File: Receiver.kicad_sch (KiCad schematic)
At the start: 45 parts, among them J2 UFL, J3 UFL, SW2 TS2306A, U1 ESP32-C3, U11 TPRT9013-33, U12 0479480001, U9 SX1280IMLTRT, Y1 40MHz, Y2 52MHz/10ppm

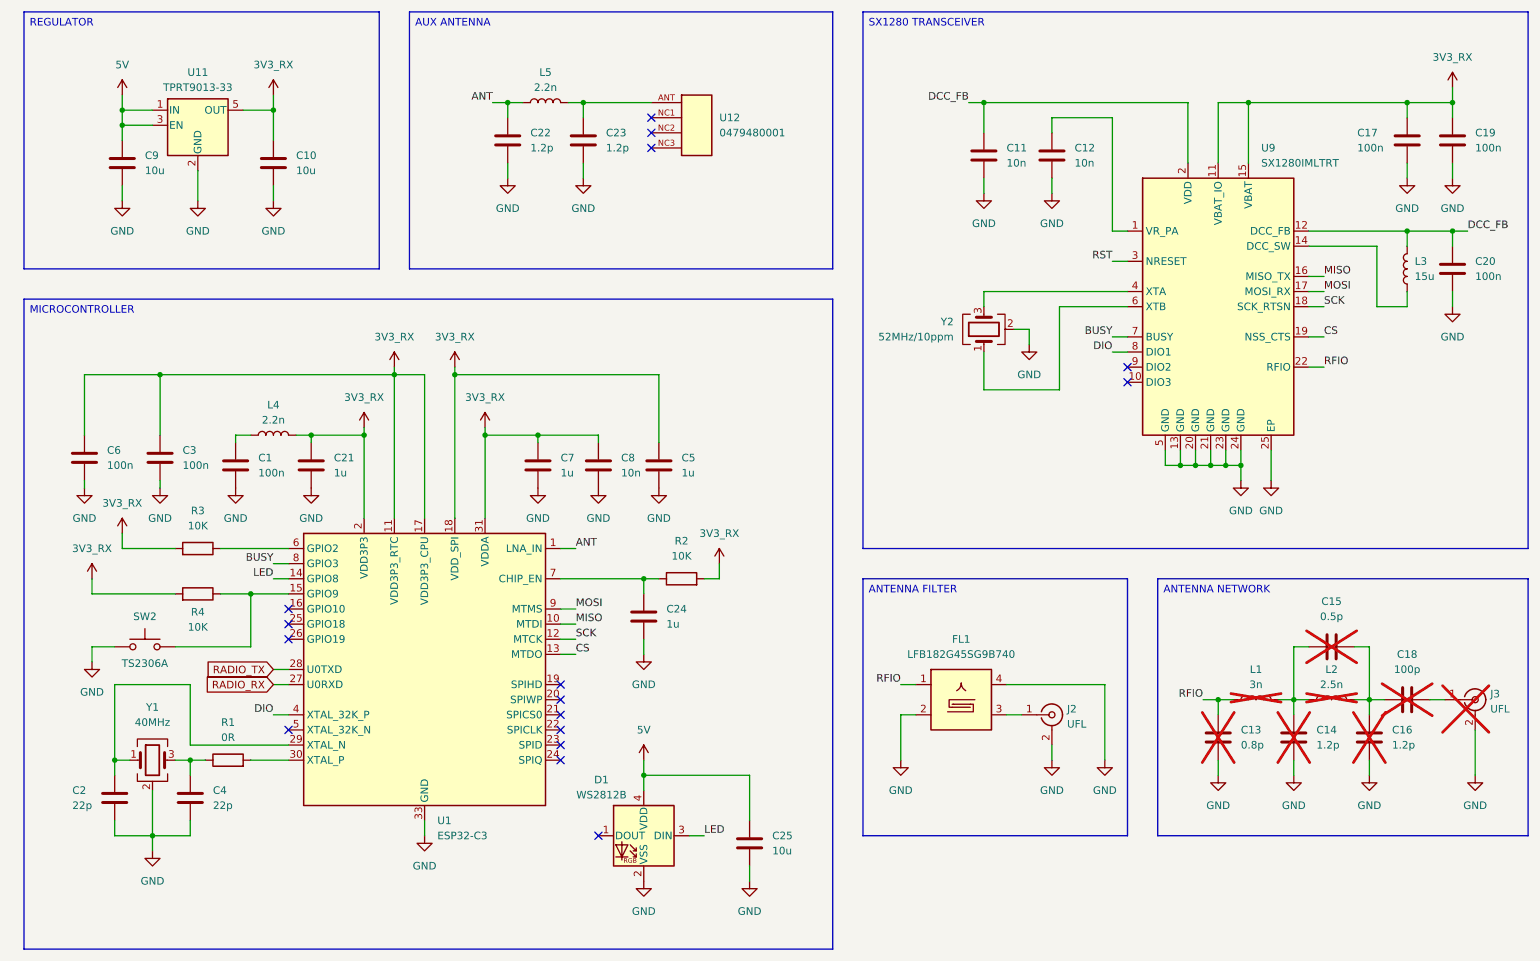
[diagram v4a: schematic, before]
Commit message: Complete ESC and MCU
Added the 4 ESC to the eschematic.
Updated the MCU design to add the connectors and buzzer.
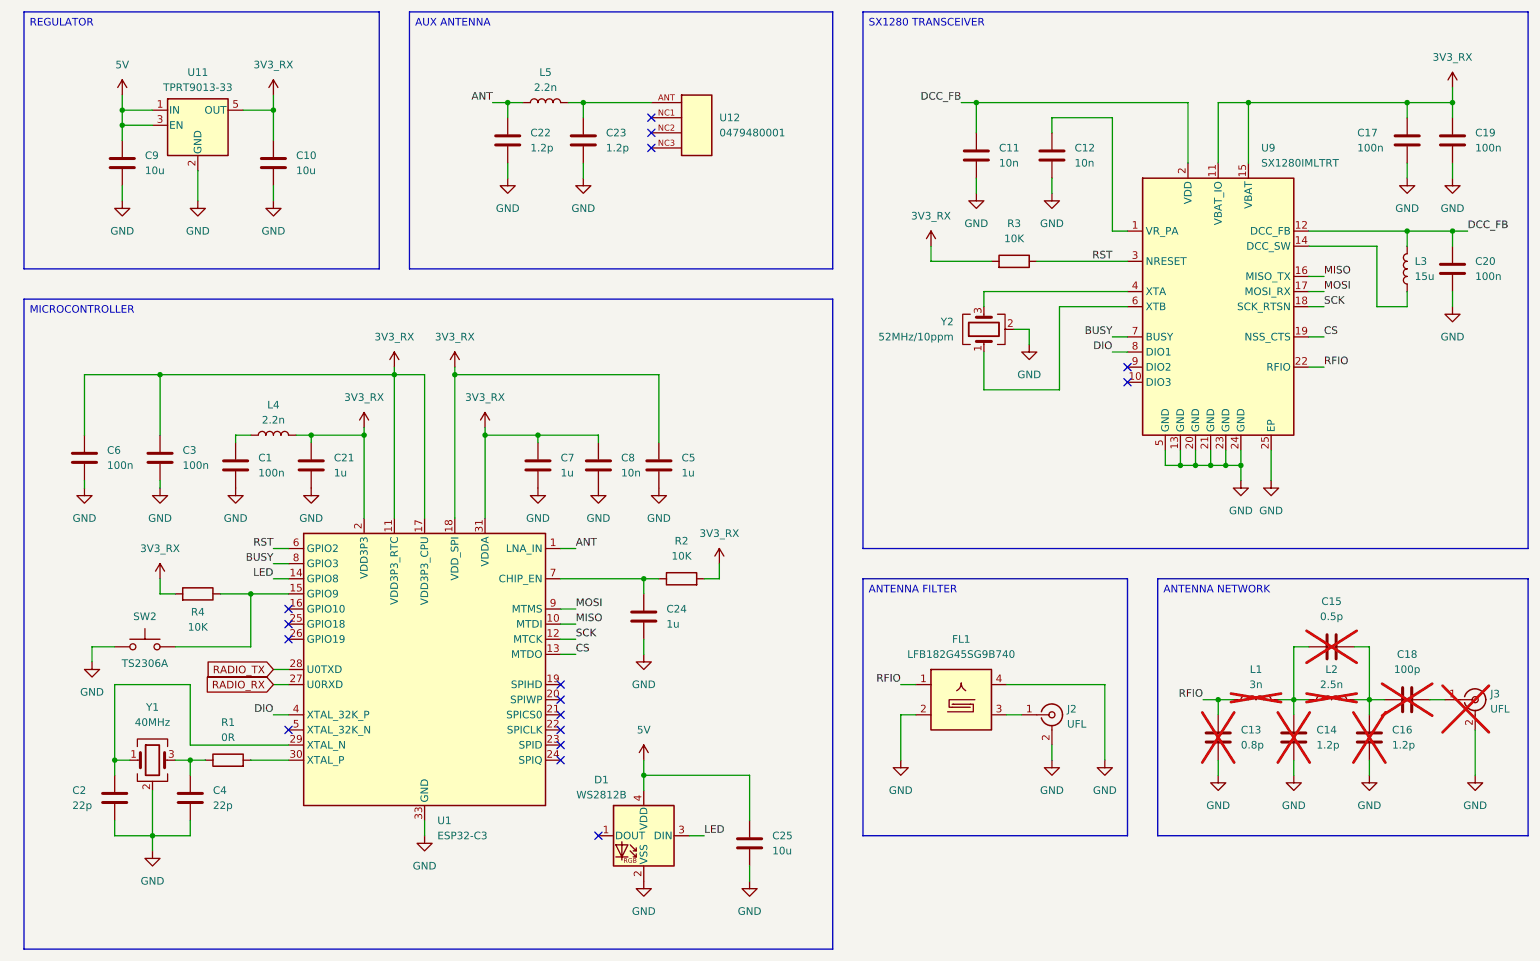
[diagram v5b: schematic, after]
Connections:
- net RST: now also R3.1, U1.6 (GPIO2)
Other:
- moved on the sheet: C11, R3
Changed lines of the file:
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@@
 	)
 	(junction
-		(at 181.61 35.56)
+		(at 180.34 35.56)
 		(diameter 0)
 		(color 0 0 0 0)
@@
 	(wire
 		(pts
+			(xy 190.5 62.23) (xy 205.74 62.23)
+		)
+		(stroke
+			(width 0)
+			(type default)
+		)
+	)
+	(wire
+		(pts
+			(xy 62.23 110.49) (xy 64.77 110.49)
+		)
+		(stroke
+			(width 0)
+			(type default)
+		)
+	)
+	(wire
+		(pts
 			(xy 114.3 38.1) (xy 114.3 35.56)
 		)
@@
 	(wire
 		(pts
-			(xy 203.2 62.23) (xy 205.74 62.23)
+			(xy 186.69 73.66) (xy 189.23 73.66)
 		)
 		(stroke
@@
 	(wire
 		(pts
-			(xy 186.69 73.66) (xy 189.23 73.66)
+			(xy 62.23 130.81) (xy 64.77 130.81)
 		)
 		(stroke
@@
 	(wire
 		(pts
-			(xy 62.23 130.81) (xy 64.77 130.81)
+			(xy 172.72 62.23) (xy 182.88 62.23)
 		)
 		(stroke
@@
 	(wire
 		(pts
-			(xy 179.07 35.56) (xy 181.61 35.56)
+			(xy 177.8 35.56) (xy 180.34 35.56)
 		)
 		(stroke
@@
 	(wire
 		(pts
-			(xy 53.34 110.49) (xy 64.77 110.49)
-		)
-		(stroke
-			(width 0)
-			(type default)
-		)
-	)
-	(wire
-		(pts
 			(xy 214.63 93.98) (xy 214.63 96.52)
 		)
@@
 	(wire
 		(pts
-			(xy 181.61 35.56) (xy 181.61 40.64)
+			(xy 180.34 35.56) (xy 180.34 40.64)
 		)
 		(stroke
@@
 	(wire
 		(pts
-			(xy 36.83 110.49) (xy 36.83 107.95)
-		)
-		(stroke
-			(width 0)
-			(type default)
-		)
-	)
-	(wire
-		(pts
 			(xy 137.16 115.57) (xy 137.16 113.03)
 		)
@@
 	(wire
 		(pts
+			(xy 172.72 62.23) (xy 172.72 59.69)
+		)
+		(stroke
+			(width 0)
+			(type default)
+		)
+	)
+	(wire
+		(pts
 			(xy 220.98 135.89) (xy 218.44 135.89)
 		)
@@
 	(wire
 		(pts
-			(xy 181.61 48.26) (xy 181.61 50.8)
+			(xy 180.34 48.26) (xy 180.34 50.8)
 		)
 		(stroke
@@
 	(wire
 		(pts
-			(xy 36.83 110.49) (xy 45.72 110.49)
-		)
-		(stroke
-			(width 0)
-			(type default)
-		)
-	)
-	(wire
-		(pts
 			(xy 62.23 113.03) (xy 64.77 113.03)
 		)
@@
 	(wire
 		(pts
-			(xy 31.75 118.11) (xy 45.72 118.11)
+			(xy 43.18 118.11) (xy 45.72 118.11)
 		)
 		(stroke
@@
 	(wire
 		(pts
-			(xy 181.61 35.56) (xy 215.9 35.56)
+			(xy 180.34 35.56) (xy 215.9 35.56)
 		)
 		(stroke
@@
 	(wire
 		(pts
-			(xy 31.75 118.11) (xy 31.75 115.57)
+			(xy 43.18 118.11) (xy 43.18 115.57)
 		)
 		(stroke
@@
 	)
 	(label "DCC_FB"
-		(at 179.07 35.56 180)
+		(at 177.8 35.56 180)
 		(effects
 			(font
@@
 		)
 	)
+	(label "RST"
+		(at 62.23 110.49 180)
+		(effects
+			(font
+				(size 1.27 1.27)
+			)
+			(justify right bottom)
+		)
+	)
 	(label "BUSY"
 		(at 203.2 74.93 180)
@@
 	(symbol
 		(lib_id "Device:C")
-		(at 181.61 44.45 0)
+		(at 180.34 44.45 0)
 		(unit 1)
 		(exclude_from_sim no)
@@
 		(fields_autoplaced yes)
 		(property "Reference" "C11"
-			(at 185.42 43.1799 0)
+			(at 184.15 43.1799 0)
 			(effects
 				(font
@@
 		)
 		(property "Value" "10n"
-			(at 185.42 45.7199 0)
+			(at 184.15 45.7199 0)
 			(effects
 				(font
@@
 		)
 		(property "Footprint" ""
-			(at 182.5752 48.26 0)
+			(at 181.3052 48.26 0)
 			(effects
 				(font
@@
 		)
 		(property "Datasheet" "~"
-			(at 181.61 44.45 0)
+			(at 180.34 44.45 0)
 			(effects
 				(font
@@
 		)
 		(property "Description" "Unpolarized capacitor"
-			(at 181.61 44.45 0)
+			(at 180.34 44.45 0)
 			(effects
 				(font
@@
 	(symbol
 		(lib_id "power:GND")
-		(at 181.61 50.8 0)
+		(at 180.34 50.8 0)
 		(unit 1)
 		(exclude_from_sim no)
@@
 		(fields_autoplaced yes)
 		(property "Reference" "#PWR017"
-			(at 181.61 57.15 0)
+			(at 180.34 57.15 0)
 			(effects
 				(font
@@
 		)
 		(property "Value" "GND"
-			(at 181.61 55.88 0)
+			(at 180.34 55.88 0)
 			(effects
 				(font
@@
 		)
 		(property "Footprint" ""
-			(at 181.61 50.8 0)
+			(at 180.34 50.8 0)
 			(effects
 				(font
@@
 		)
 		(property "Datasheet" ""
-			(at 181.61 50.8 0)
+			(at 180.34 50.8 0)
 			(effects
 				(font
@@
 		)
 		(property "Description" "Power symbol creates a global label with name \"GND\" , ground"
-			(at 181.61 50.8 0)
+			(at 180.34 50.8 0)
 			(effects
 				(font
@@
 	(symbol
 		(lib_id "Device:R")
-		(at 49.53 110.49 270)
+		(at 186.69 62.23 270)
 		(mirror x)
 		(unit 1)
@@
 		(fields_autoplaced yes)
 		(property "Reference" "R3"
-			(at 49.53 104.14 90)
+			(at 186.69 55.88 90)
 			(effects
 				(font
@@
 		)
 		(property "Value" "10K"
-			(at 49.53 106.68 90)
+			(at 186.69 58.42 90)
 			(effects
 				(font
@@
 		)
 		(property "Footprint" ""
-			(at 49.53 112.268 90)
+			(at 186.69 64.008 90)
 			(effects
 				(font
@@
 		)
 		(property "Datasheet" "~"
-			(at 49.53 110.49 0)
+			(at 186.69 62.23 0)
 			(effects
 				(font
@@
 		)
 		(property "Description" "Resistor"
-			(at 49.53 110.49 0)
+			(at 186.69 62.23 0)
 			(effects
 				(font
@@
 		)
 		(instances
-			(project "Receiver"
-				(path "/073b6cc7-6d76-466f-8a69-83af0ccbf374"
-					(reference "R2")
-					(unit 1)
-				)
-			)
 			(project "ThunderHorse"
 				(path "/ac187c6c-fa53-41cc-bce1-6f39a42a92e8/bc3cf81e-9940-4196-8a64-4d021e41ea8d"
@@
 	(symbol
 		(lib_id "power:+3V3")
-		(at 31.75 115.57 0)
+		(at 43.18 115.57 0)
 		(unit 1)
 		(exclude_from_sim no)
@@
 		(dnp no)
 		(property "Reference" "#PWR046"
-			(at 31.75 119.38 0)
+			(at 43.18 119.38 0)
 			(effects
 				(font
@@
 		)
 		(property "Value" "3V3_RX"
-			(at 31.75 110.49 0)
+			(at 43.18 110.49 0)
 			(effects
 				(font
@@
 		)
 		(property "Footprint" ""
-			(at 31.75 115.57 0)
+			(at 43.18 115.57 0)
 			(effects
 				(font
@@
 		)
 		(property "Datasheet" ""
-			(at 31.75 115.57 0)
+			(at 43.18 115.57 0)
 			(effects
 				(font
@@
 		)
 		(property "Description" "Power symbol creates a global label with name \"+3V3\""
-			(at 31.75 115.57 0)
+			(at 43.18 115.57 0)
 			(effects
 				(font
@@
 	(symbol
 		(lib_id "power:+3V3")
-		(at 36.83 107.95 0)
+		(at 172.72 59.69 0)
 		(unit 1)
 		(exclude_from_sim no)
@@
 		(dnp no)
 		(property "Reference" "#PWR039"
-			(at 36.83 111.76 0)
+			(at 172.72 63.5 0)
 			(effects
 				(font
@@
 		)
 		(property "Value" "3V3_RX"
-			(at 36.83 102.87 0)
+			(at 172.72 54.61 0)
 			(effects
 				(font
@@
 		)
 		(property "Footprint" ""
-			(at 36.83 107.95 0)
+			(at 172.72 59.69 0)
 			(effects
 				(font
@@
 		)
 		(property "Datasheet" ""
-			(at 36.83 107.95 0)
+			(at 172.72 59.69 0)
 			(effects
 				(font
@@
 		)
 		(property "Description" "Power symbol creates a global label with name \"+3V3\""
-			(at 36.83 107.95 0)
+			(at 172.72 59.69 0)
 			(effects
 				(font

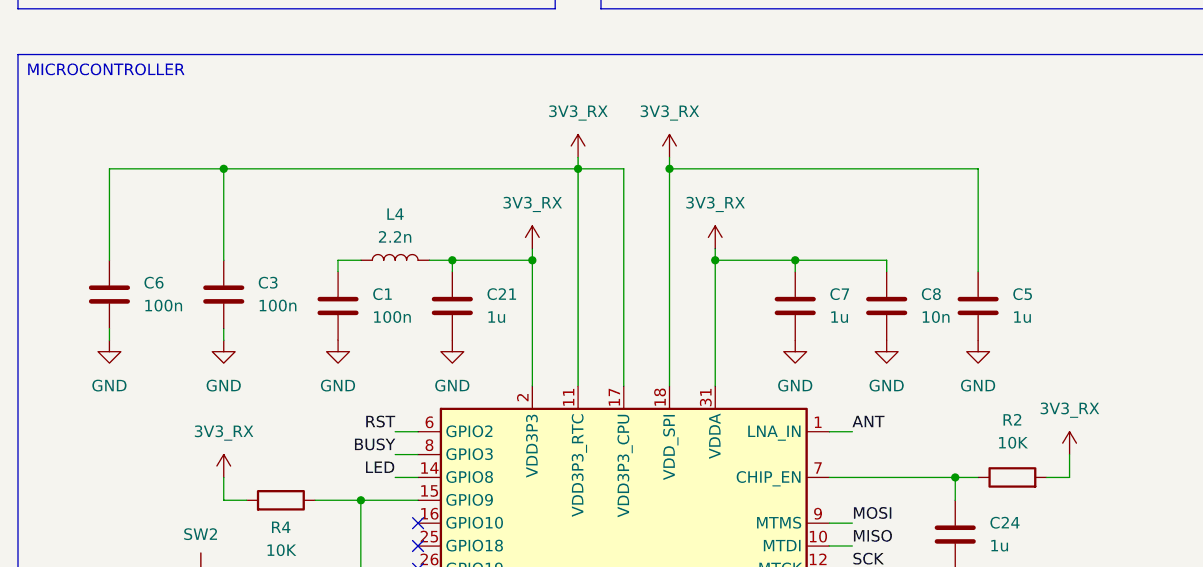
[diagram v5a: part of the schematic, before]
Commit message: Power design
Added the 5V regulator schematic.
Updated the MCU schematic.
Updated the RX schematic.
Updated the sensors schematic.

TODO:
Calculate the voltage divider for the 5V regulator.
Review all connections and systems.
Select the footprints for the missing components.
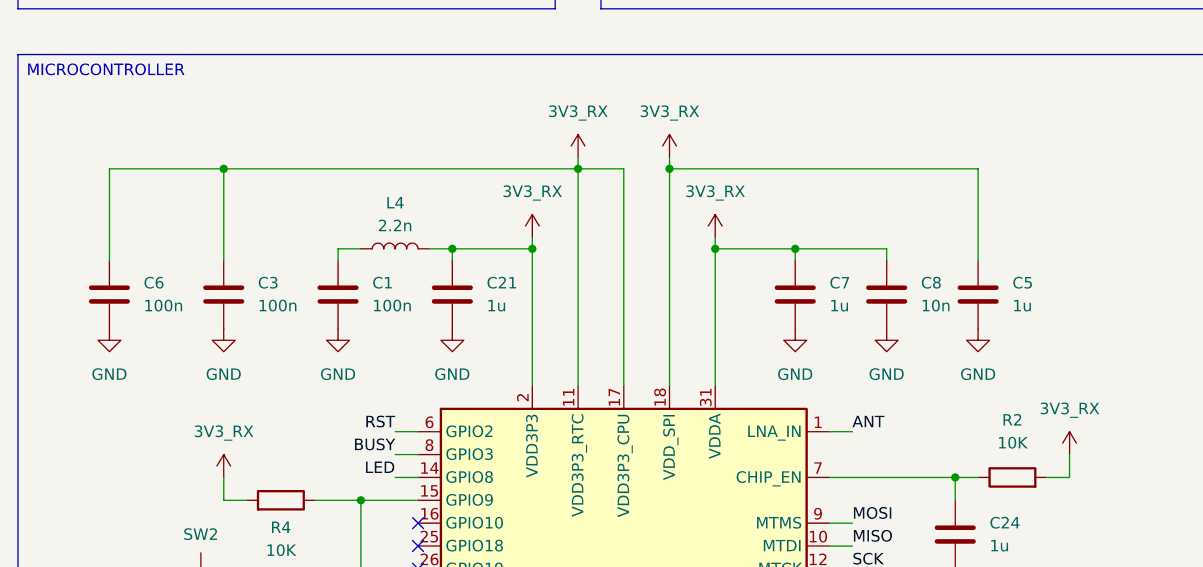
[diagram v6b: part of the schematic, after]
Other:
- moved on the sheet: C1, C21, C5, C7, C8, L4
